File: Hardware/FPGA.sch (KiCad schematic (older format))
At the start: 25 parts, among them U501 W25Q128JVxxM, U502 ICE40UP5K-SG48, U503 Crystal Oscillator, U504 USBLC6-2

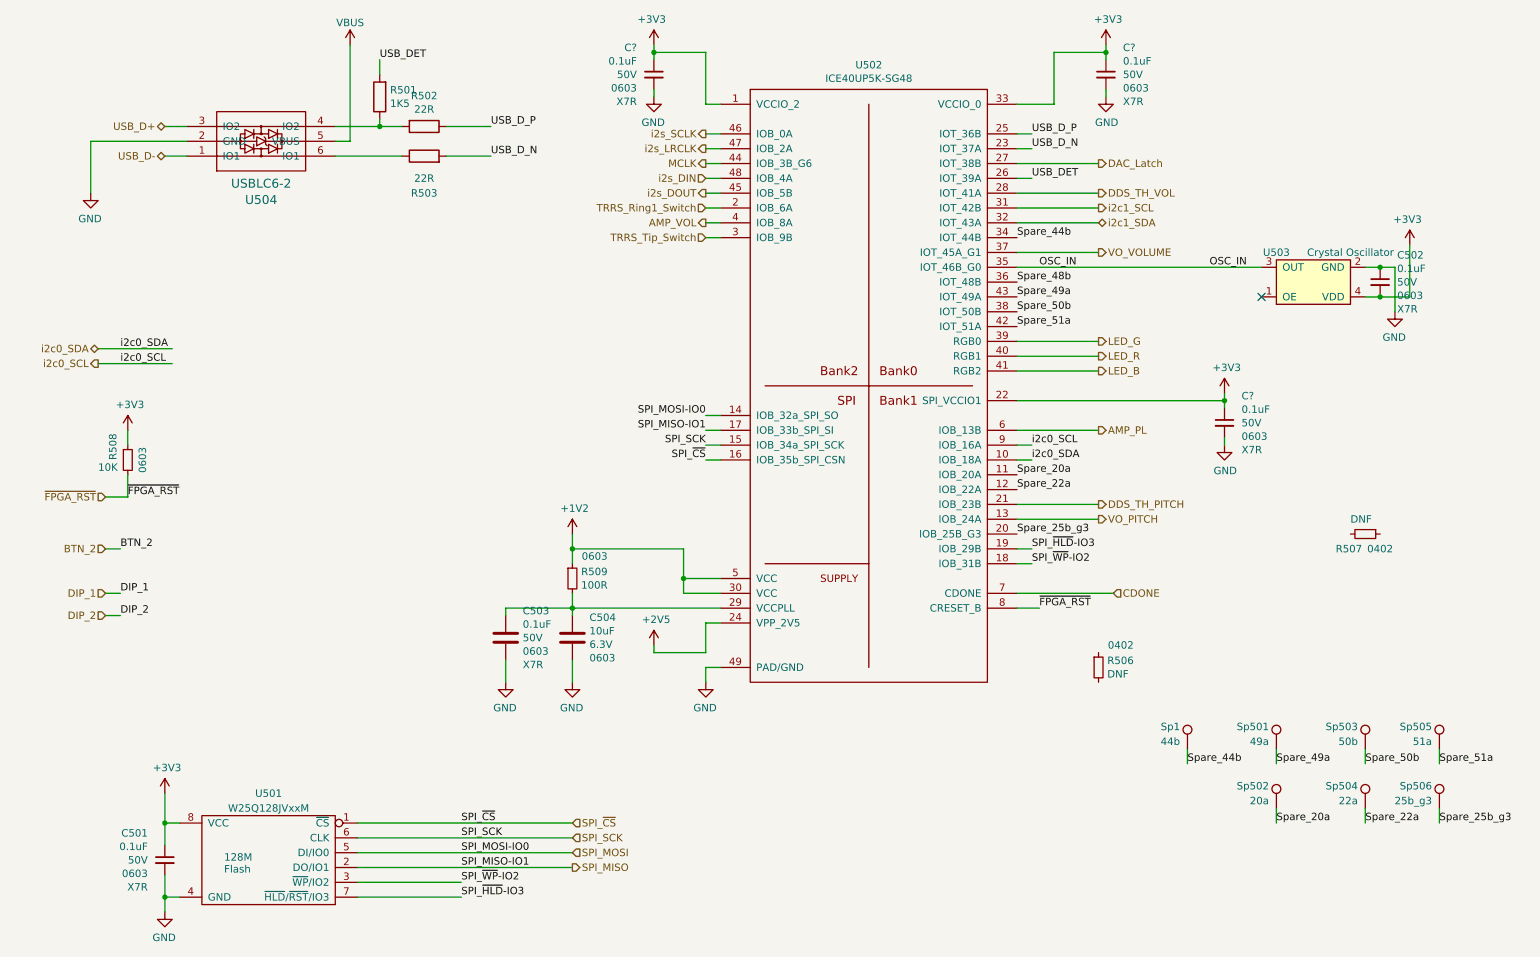
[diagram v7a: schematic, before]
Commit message: Changing off slide switch for unpopulated TH.
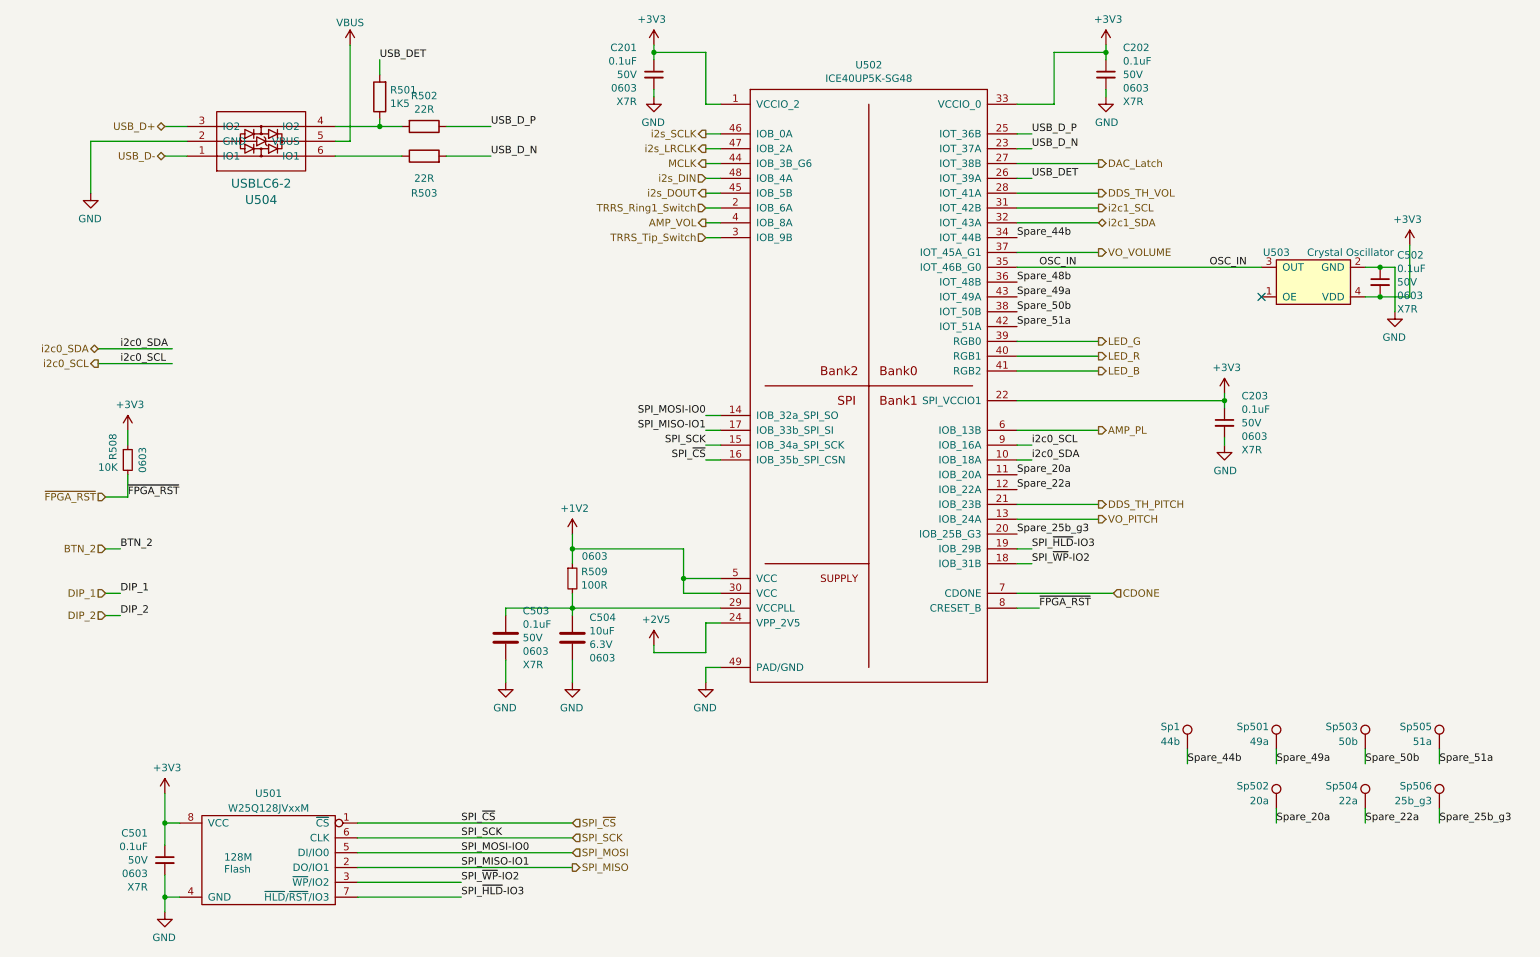
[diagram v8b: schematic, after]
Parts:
- removed R506, R507: DNF, Resistor_SMD:R_0402_1005Metric, symbol Device:R_Small
- gave numbers to parts that had none: 3
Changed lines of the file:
@@
 Wire Wire Line
 	1750 3000 1250 3000
-$Comp
-L Device:R_Small R?
-U 1 1 615CF009
-P 8000 5050
-AR Path="/611E335F/615CF009" Ref="R?"  Part="1"
-AR Path="/615CF009" Ref="R?"  Part="1"
-AR Path="/611E3335/615CF009" Ref="R506"  Part="1"
-F 0 "R506" H 8059 5096 50  0000 L CNN
-F 1 "DNF" H 8059 5005 50  0000 L CNN
-F 2 "Resistor_SMD:R_0402_1005Metric" V 7930 5050 50  0001 C CNN
-F 3 "~" H 8000 5050 50  0001 C CNN
-F 4 "0402" H 8150 5200 50  0000 C CNN "Pkg"
-F 5 "" H 8000 5050 50  0001 C CNN "MPN"
-F 6 "" H 8000 5050 50  0001 C CNN "DPN"
-	1    8000 5050
-	1    0    0    -1
-$EndComp
-$Comp
-L Device:R_Small R?
-U 1 1 615D7F58
-P 9800 4150
-AR Path="/611E335F/615D7F58" Ref="R?"  Part="1"
-AR Path="/615D7F58" Ref="R?"  Part="1"
-AR Path="/611E3335/615D7F58" Ref="R507"  Part="1"
-F 0 "R507" V 9900 3950 50  0000 L CNN
-F 1 "DNF" V 9700 4050 50  0000 L CNN
-F 2 "Resistor_SMD:R_0402_1005Metric" V 9730 4150 50  0001 C CNN
-F 3 "~" H 9800 4150 50  0001 C CNN
-F 4 "0402" V 9900 4250 50  0000 C CNN "Pkg"
-F 5 "" H 9800 4150 50  0001 C CNN "MPN"
-F 6 "" H 9800 4150 50  0001 C CNN "DPN"
-	1    9800 4150
-	0    1    1    0
-$EndComp
 Text HLabel 5350 2050 0    50   Output ~ 0
 AMP_VOL
@@
 P 5000 1050
 AR Path="/611E335F/61497B20" Ref="C?"  Part="1"
-AR Path="/611E3335/61497B20" Ref="C?"  Part="1"
-F 0 "C?" H 5115 1232 50  0000 L CNN
+AR Path="/611E3335/61497B20" Ref="C201"  Part="1"
+F 0 "C201" H 5115 1232 50  0000 L CNN
 F 1 "0.1uF" H 5115 1141 50  0000 L CNN
 F 2 "Capacitor_SMD:C_0603_1608Metric" H 5038 900 50  0001 C CNN
@@
 $EndComp
 $Comp
-L power:GND #PWR?
+L power:GND #PWR0170
 U 1 1 6149AB04
 P 5000 1200
-F 0 "#PWR?" H 5000 950 50  0001 C CNN
+F 0 "#PWR0170" H 5000 950 50  0001 C CNN
 F 1 "GND" H 5005 1027 50  0000 C CNN
 F 2 "" H 5000 1200 50  0001 C CNN
@@
 	5000 900  5000 950
 $Comp
-L power:+3V3 #PWR?
+L power:+3V3 #PWR0186
 U 1 1 614A844D
 P 8050 850
-F 0 "#PWR?" H 8050 700 50  0001 C CNN
+F 0 "#PWR0186" H 8050 700 50  0001 C CNN
 F 1 "+3V3" H 8065 1023 50  0000 C CNN
 F 2 "" H 8050 850 50  0001 C CNN
@@
 P 8050 1050
 AR Path="/611E335F/614A8458" Ref="C?"  Part="1"
-AR Path="/611E3335/614A8458" Ref="C?"  Part="1"
-F 0 "C?" H 8165 1232 50  0000 L CNN
+AR Path="/611E3335/614A8458" Ref="C202"  Part="1"
+F 0 "C202" H 8165 1232 50  0000 L CNN
 F 1 "0.1uF" H 8165 1141 50  0000 L CNN
 F 2 "Capacitor_SMD:C_0603_1608Metric" H 8088 900 50  0001 C CNN
@@
 $EndComp
 $Comp
-L power:GND #PWR?
+L power:GND #PWR0187
 U 1 1 614A845E
 P 8050 1200
-F 0 "#PWR?" H 8050 950 50  0001 C CNN
+F 0 "#PWR0187" H 8050 950 50  0001 C CNN
 F 1 "GND" H 8055 1027 50  0000 C CNN
 F 2 "" H 8050 1200 50  0001 C CNN
@@
 	7700 1250 7450 1250
 $Comp
-L power:+3V3 #PWR?
+L power:+3V3 #PWR0188
 U 1 1 614B4975
 P 8850 3200
-F 0 "#PWR?" H 8850 3050 50  0001 C CNN
+F 0 "#PWR0188" H 8850 3050 50  0001 C CNN
 F 1 "+3V3" H 8865 3373 50  0000 C CNN
 F 2 "" H 8850 3200 50  0001 C CNN
@@
 P 8850 3400
 AR Path="/611E335F/614B4980" Ref="C?"  Part="1"
-AR Path="/611E3335/614B4980" Ref="C?"  Part="1"
-F 0 "C?" H 8965 3582 50  0000 L CNN
+AR Path="/611E3335/614B4980" Ref="C203"  Part="1"
+F 0 "C203" H 8965 3582 50  0000 L CNN
 F 1 "0.1uF" H 8965 3491 50  0000 L CNN
 F 2 "Capacitor_SMD:C_0603_1608Metric" H 8888 3250 50  0001 C CNN
@@
 $EndComp
 $Comp
-L power:GND #PWR?
+L power:GND #PWR0189
 U 1 1 614B4986
 P 8850 3550
-F 0 "#PWR?" H 8850 3300 50  0001 C CNN
+F 0 "#PWR0189" H 8850 3300 50  0001 C CNN
 F 1 "GND" H 8855 3377 50  0000 C CNN
 F 2 "" H 8850 3550 50  0001 C CNN
